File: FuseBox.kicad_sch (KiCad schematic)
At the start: 2 parts

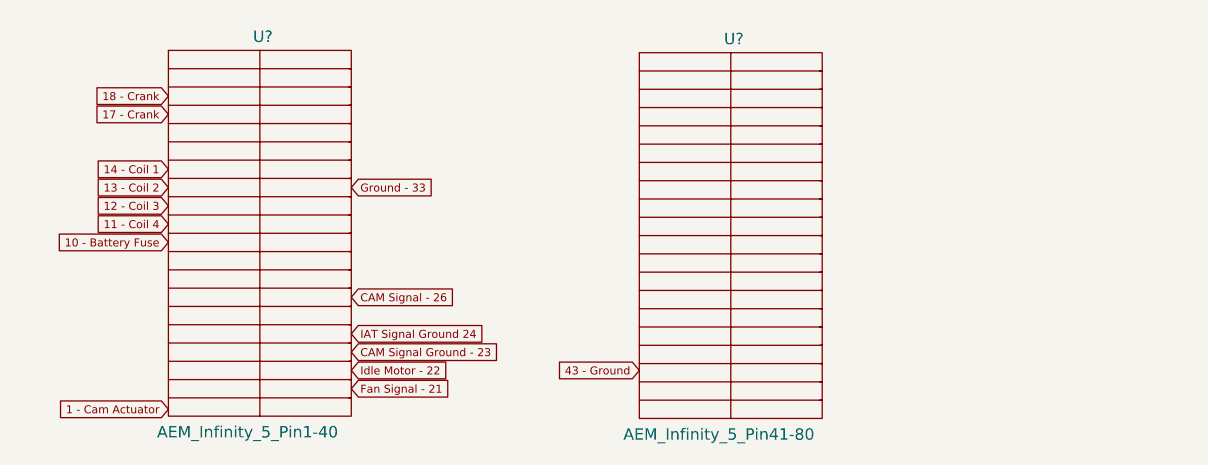
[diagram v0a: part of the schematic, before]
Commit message: More ECU pins
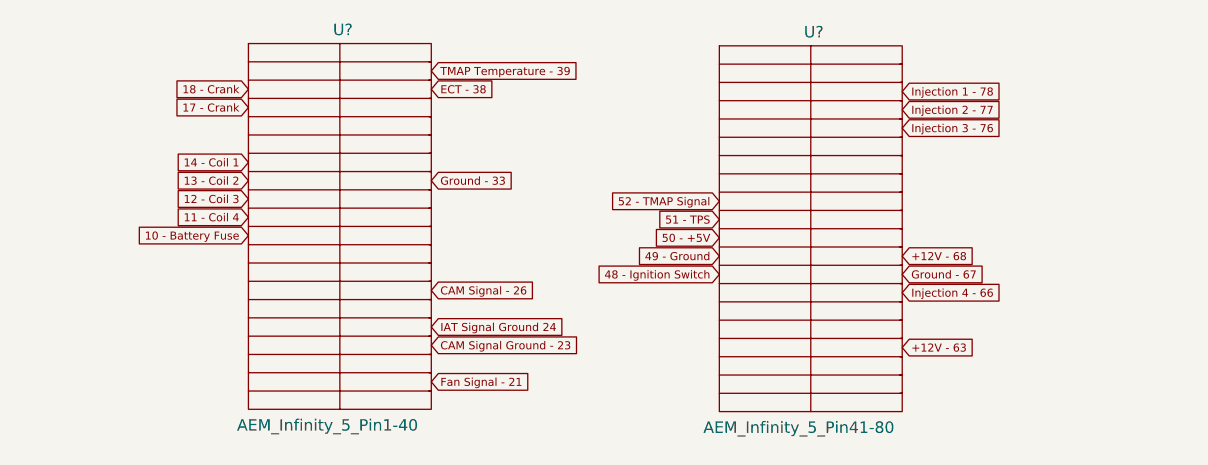
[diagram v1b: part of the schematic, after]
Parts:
- removed U?: AEM_Infinity_5_Pin1-40, symbol SCR23 Library:AEM_Infinity_5_Pin1-40
- removed U?: AEM_Infinity_5_Pin41-80, symbol SCR23 Library:AEM_Infinity_5_Pin41-80
- added U?: AEM_Infinity_5_Pin41-80, symbol SCR23 Library:AEM_Infinity_5_Pin41-80
- added U?: AEM_Infinity_5_Pin1-40, symbol SCR23 Library:AEM_Infinity_5_Pin1-40

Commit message: Created subschematics that Jack drew
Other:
- added sheet Charging System (Charging-System.kicad_sch)
- added sheet DTM Dash (DTM-Dash.kicad_sch)
- added sheet ECU Main Loom (ECU-Main-Loom.kicad_sch)
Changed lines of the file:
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@@
     )
   )
-  (sheet (at 232.918 69.342) (size 20.574 16.002) (fields_autoplaced)
+  (sheet (at 202.946 45.974) (size 20.066 13.716) (fields_autoplaced)
     (stroke (width 0.1524) (type solid) (color 0 0 0 0))
     (fill (color 0 0 0 0.0000))
-    (property "Sheet name" "Fuse Box Schematic" (id 0) (at 232.918 68.6304 0)
+    (property "Sheet name" "ECU Main Loom" (id 0) (at 202.946 45.2624 0)
       (effects (font (size 1.27 1.27)) (justify left bottom))
     )
-    (property "Sheet file" "FuseBoxSchematic(1).kicad_sch" (id 1) (at 232.918 85.9286 0)
+    (property "Sheet file" "ECU-Main-Loom.kicad_sch" (id 1) (at 202.946 60.2746 0)
       (effects (font (size 1.27 1.27)) (justify left top))
     )
+  )
+  (sheet (at 202.946 25.4) (size 20.066 12.954) (fields_autoplaced)
+    (stroke (width 0.1524) (type solid) (color 0 0 0 0))
+    (fill (color 0 0 0 0.0000))
+    (property "Sheet name" "Fuse Box Schematic" (id 0) (at 202.946 24.6884 0)
+      (effects (font (size 1.27 1.27)) (justify left bottom))
+    )
+    (property "Sheet file" "FuseBoxSchematic(1).kicad_sch" (id 1) (at 202.946 38.9386 0)
+      (effects (font (size 1.27 1.27)) (justify left top))
+    )
+  )
+  (sheet (at 202.946 66.04) (size 20.066 14.986) (fields_autoplaced)
+    (stroke (width 0.1524) (type solid) (color 0 0 0 0))
+    (fill (color 0 0 0 0.0000))
+    (property "Sheet name" "Charging System" (id 0) (at 202.946 65.3284 0)
+      (effects (font (size 1.27 1.27)) (justify left bottom))
+    )
+    (property "Sheet file" "Charging-System.kicad_sch" (id 1) (at 202.946 81.6106 0)
+      (effects (font (size 1.27 1.27)) (justify left top))
+    )
+  )
+  (sheet (at 203.2 87.63) (size 19.812 12.446) (fields_autoplaced)
+    (stroke (width 0.1524) (type solid) (color 0 0 0 0))
+    (fill (color 0 0 0 0.0000))
+    (property "Sheet name" "DTM Dash" (id 0) (at 203.2 86.9184 0)
+      (effects (font (size 1.27 1.27)) (justify left bottom))
+    )
+    (property "Sheet file" "DTM-Dash.kicad_sch" (id 1) (at 203.2 100.6606 0)
+      (effects (font (size 1.27 1.27)) (justify left top))
+    )

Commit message: fix everything
shid
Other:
- added sheet Coil Overview (Coil_Overview.kicad_sch)
- added sheet Engine Overview (Engine.kicad_sch)
- moved on the sheet: U?
